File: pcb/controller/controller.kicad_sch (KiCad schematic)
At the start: 38 parts, among them J1 Barrel_Jack, J2 AVR-ISP-6, Q1 2N7002, U1 ATmega328P-A, Y1 Crystal_GND24

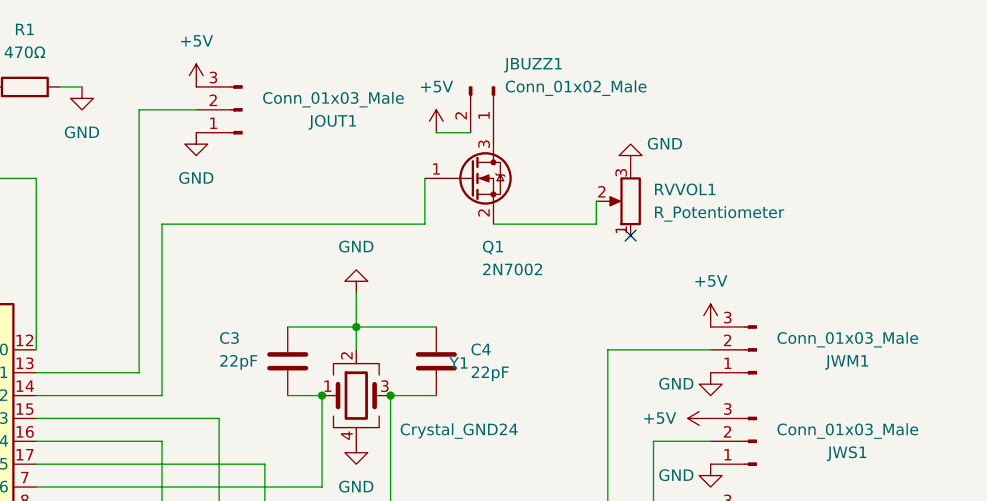
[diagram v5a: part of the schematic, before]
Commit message: PCB Touchup
Two changes in this commit.

1. I rewired the volume potentiometer so that the MOSFET is now the
closest thing to ground.  That way we'll always be sure to have
sufficient gate-source voltage to trigger it when the buzzer is turned
on.

2. I added v1/date indicators to the silk screen layers of all the
PCBs.
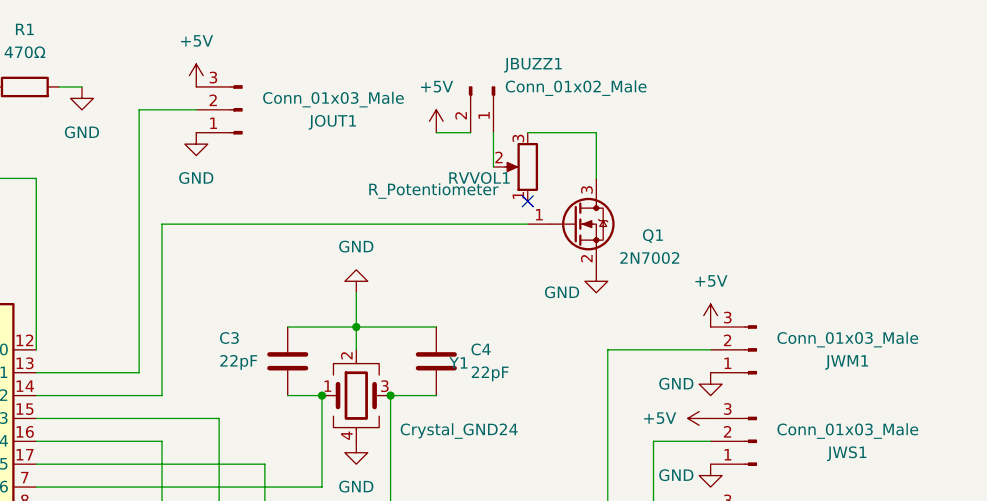
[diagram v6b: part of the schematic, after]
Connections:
- net GND: now also Q1.2 (S); no longer RVVOL1.3
- net at RVVOL1.2: now also JBUZZ1.1 (Pin_1); no longer Q1.2 (S)
- net at Q1.3 (D): now also RVVOL1.3; no longer JBUZZ1.1 (Pin_1)
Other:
- moved on the sheet: Q1, RVVOL1
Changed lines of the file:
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@@
   (junction (at 92.71 181.61) (diameter 0) (color 0 0 0 0)
   )
-  (no_connect (at 158.75 38.1))
+  (no_connect (at 147.32 34.29))
   (no_connect (at 25.4 50.8))
   (no_connect (at 62.23 58.42))
@@
     (stroke (width 0) (type default) (color 0 0 0 0))
   )
-  (wire (pts (xy 154.94 36.83) (xy 154.94 34.29))
-    (stroke (width 0) (type default) (color 0 0 0 0))
-  )
   (wire (pts (xy 124.46 128.27) (xy 121.92 128.27))
     (stroke (width 0) (type default) (color 0 0 0 0))
@@
     (stroke (width 0) (type default) (color 0 0 0 0))
   )
+  (wire (pts (xy 147.32 26.67) (xy 154.94 26.67))
+    (stroke (width 0) (type default) (color 0 0 0 0))
+  )
   (wire (pts (xy 106.68 156.21) (xy 106.68 162.56))
     (stroke (width 0) (type default) (color 0 0 0 0))
@@
     (stroke (width 0) (type default) (color 0 0 0 0))
   )
-  (wire (pts (xy 143.51 36.83) (xy 154.94 36.83))
-    (stroke (width 0) (type default) (color 0 0 0 0))
-  )
   (wire (pts (xy 132.08 68.58) (xy 132.08 55.88))
     (stroke (width 0) (type default) (color 0 0 0 0))
@@
     (stroke (width 0) (type default) (color 0 0 0 0))
   )
-  (wire (pts (xy 135.89 36.83) (xy 135.89 31.75))
+  (wire (pts (xy 143.51 26.67) (xy 143.51 30.48))
     (stroke (width 0) (type default) (color 0 0 0 0))
   )
@@
     (stroke (width 0) (type default) (color 0 0 0 0))
   )
+  (wire (pts (xy 154.94 26.67) (xy 154.94 31.75))
+    (stroke (width 0) (type default) (color 0 0 0 0))
+  )
   (wire (pts (xy 114.3 147.32) (xy 110.49 147.32))
     (stroke (width 0) (type default) (color 0 0 0 0))
@@
     (stroke (width 0) (type default) (color 0 0 0 0))
   )
-  (wire (pts (xy 106.68 36.83) (xy 135.89 36.83))
+  (wire (pts (xy 106.68 36.83) (xy 147.32 36.83))
     (stroke (width 0) (type default) (color 0 0 0 0))
   )
@@
     (pin "2")
   )
-  (symbol (lib_id "Device:R_Potentiometer") (at 158.75 34.29 180) (unit 1)
-    (in_bom yes) (on_board yes)
-    (property "Reference" "RVVOL1" (id 0) (at 161.29 33.0199 0)
+  (symbol (lib_id "Device:R_Potentiometer") (at 147.32 30.48 180) (unit 1)
+    (in_bom yes) (on_board yes)
+    (property "Reference" "RVVOL1" (id 0) (at 138.43 31.75 0)
       (effects (font (size 1.27 1.27)) (justify right))
     )
-    (property "Value" "R_Potentiometer" (id 1) (at 161.29 35.5599 0)
+    (property "Value" "R_Potentiometer" (id 1) (at 129.54 33.02 0)
       (effects (font (size 1.27 1.27)) (justify right))
     )
-    (property "Footprint" "Potentiometer_THT:Potentiometer_Bourns_3386P_Vertical" (id 2) (at 158.75 34.29 0)
-      (effects (font (size 1.27 1.27)) hide)
-    )
-    (property "Datasheet" "~" (id 3) (at 158.75 34.29 0)
+    (property "Footprint" "Potentiometer_THT:Potentiometer_Bourns_3386P_Vertical" (id 2) (at 147.32 30.48 0)
+      (effects (font (size 1.27 1.27)) hide)
+    )
+    (property "Datasheet" "~" (id 3) (at 147.32 30.48 0)
       (effects (font (size 1.27 1.27)) hide)
     )
@@
     (pin "1")
   )
-  (symbol (lib_id "Transistor_FET:2N7002") (at 140.97 31.75 0) (unit 1)
-    (in_bom yes) (on_board yes)
-    (property "Reference" "Q1" (id 0) (at 142.24 39.37 0)
-      (effects (font (size 1.27 1.27)) (justify left))
-    )
-    (property "Value" "2N7002" (id 1) (at 142.24 41.91 0)
-      (effects (font (size 1.27 1.27)) (justify left))
-    )
-    (property "Footprint" "Package_TO_SOT_SMD:SOT-23" (id 2) (at 146.05 33.655 0)
+  (symbol (lib_id "Transistor_FET:2N7002") (at 152.4 36.83 0) (unit 1)
+    (in_bom yes) (on_board yes)
+    (property "Reference" "Q1" (id 0) (at 160.02 38.1 0)
+      (effects (font (size 1.27 1.27)) (justify left))
+    )
+    (property "Value" "2N7002" (id 1) (at 157.48 40.64 0)
+      (effects (font (size 1.27 1.27)) (justify left))
+    )
+    (property "Footprint" "Package_TO_SOT_SMD:SOT-23" (id 2) (at 157.48 38.735 0)
       (effects (font (size 1.27 1.27) italic) (justify left) hide)
     )
-    (property "Datasheet" "https://www.onsemi.com/pub/Collateral/NDS7002A-D.PDF" (id 3) (at 140.97 31.75 0)
+    (property "Datasheet" "https://www.onsemi.com/pub/Collateral/NDS7002A-D.PDF" (id 3) (at 152.4 36.83 0)
       (effects (font (size 1.27 1.27)) (justify left) hide)
     )
-    (property "LCSC" "C8545" (id 4) (at 140.97 31.75 0)
+    (property "LCSC" "C8545" (id 4) (at 152.4 36.83 0)
       (effects (font (size 1.27 1.27)) hide)
     )
@@
     (pin "1")
   )
-  (symbol (lib_id "power:GND") (at 158.75 30.48 180) (unit 1)
-    (in_bom yes) (on_board yes)
-    (property "Reference" "#PWR0140" (id 0) (at 158.75 24.13 0)
-      (effects (font (size 1.27 1.27)) hide)
-    )
-    (property "Value" "GND" (id 1) (at 162.56 27.94 0))
-    (property "Footprint" "" (id 2) (at 158.75 30.48 0)
-      (effects (font (size 1.27 1.27)) hide)
-    )
-    (property "Datasheet" "" (id 3) (at 158.75 30.48 0)
-      (effects (font (size 1.27 1.27)) hide)
-    )
+  (symbol (lib_id "power:GND") (at 154.94 41.91 0) (unit 1)
+    (in_bom yes) (on_board yes)
+    (property "Reference" "#PWR0140" (id 0) (at 154.94 48.26 0)
+      (effects (font (size 1.27 1.27)) hide)
+    )
+    (property "Value" "GND" (id 1) (at 151.13 44.45 0))
+    (property "Footprint" "" (id 2) (at 154.94 41.91 0)
+      (effects (font (size 1.27 1.27)) hide)
+    )
+    (property "Datasheet" "" (id 3) (at 154.94 41.91 0)
+      (effects (font (size 1.27 1.27)) hide)
+    )

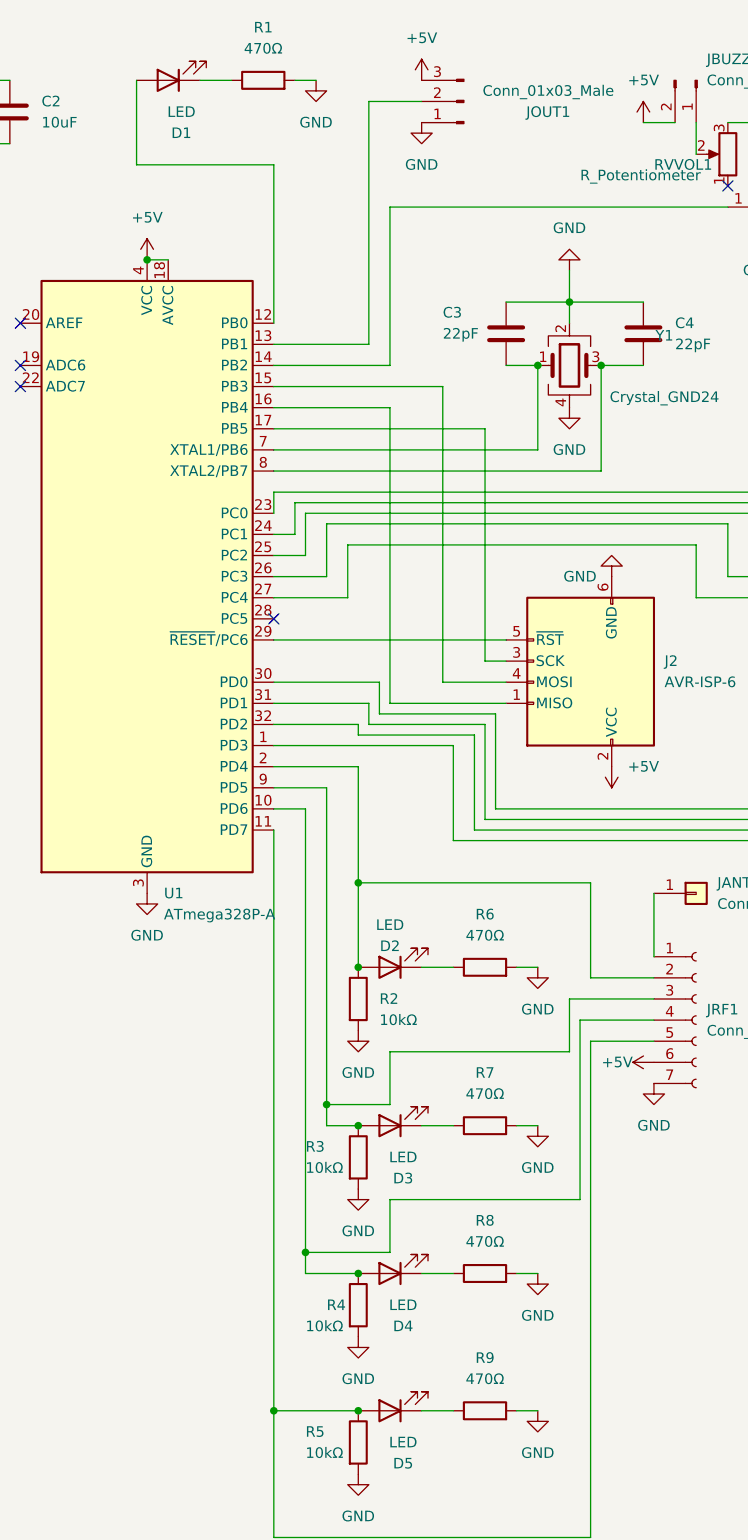
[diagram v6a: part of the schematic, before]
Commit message: Bump Up LED Resistors
The LEDs on the controller board are very bright in the first batch of
boards, so this replaces the 470ohm resistors with 1k resistors to dim
them a little.
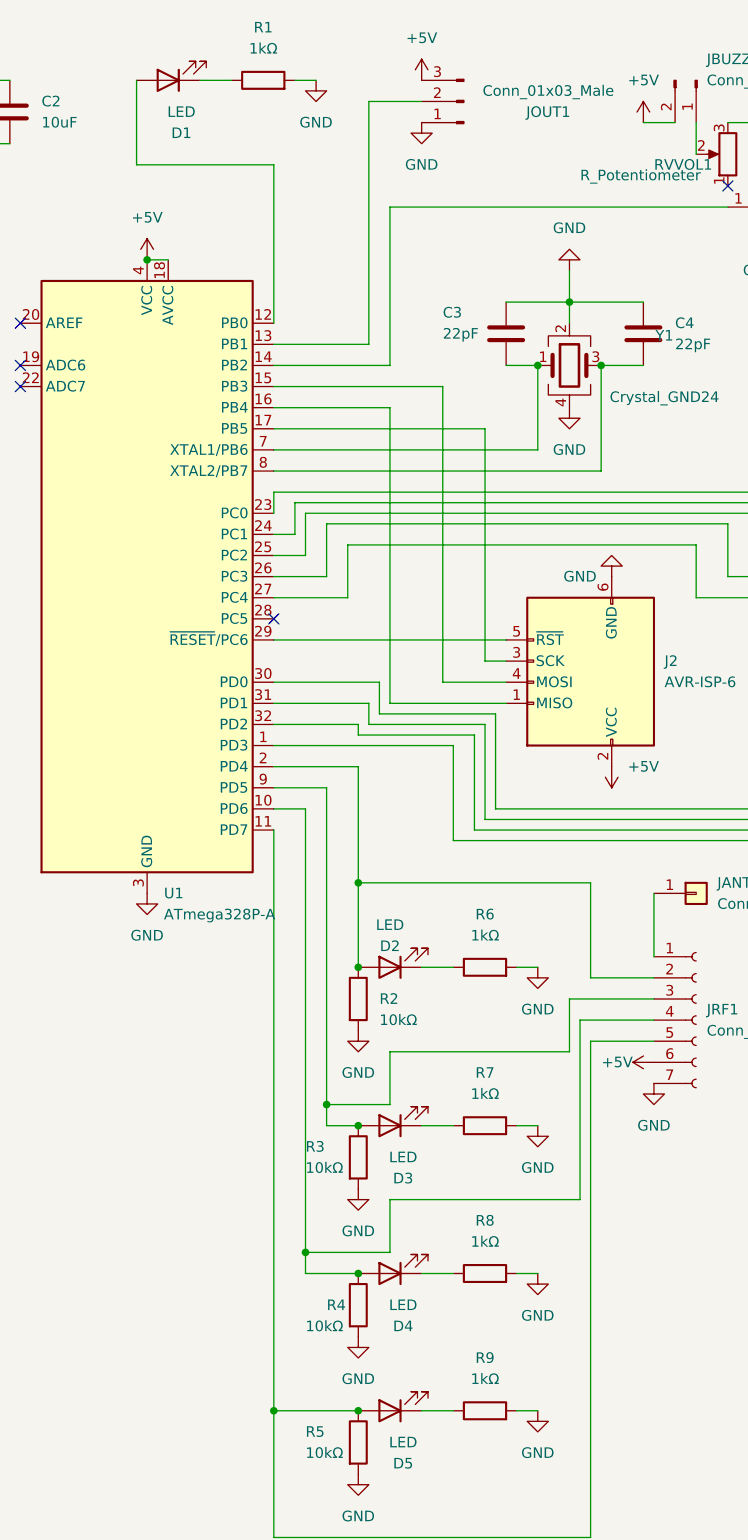
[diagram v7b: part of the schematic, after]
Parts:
- R1, R6, R7, R8, R9: value 470Ω -> 1kΩ; footprint Resistor_SMD:R_0805_2012Metric -> Resistor_SMD:R_0603_1608Metric; LCSC C17710 -> C21190
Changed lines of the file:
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@@
     (pin "3")
+  )
+  (symbol (lib_id "Device:R") (at 118.11 128.27 90) (unit 1)
+    (in_bom yes) (on_board yes) (fields_autoplaced)
+    (property "Reference" "R6" (id 0) (at 118.11 121.92 90))
+    (property "Value" "1kΩ" (id 1) (at 118.11 124.46 90))
+    (property "Footprint" "Resistor_SMD:R_0603_1608Metric" (id 2) (at 118.11 130.048 90)
+      (effects (font (size 1.27 1.27)) hide)
+    )
+    (property "Datasheet" "~" (id 3) (at 118.11 128.27 0)
+      (effects (font (size 1.27 1.27)) hide)
+    )
+    (property "LCSC" "C21190" (id 4) (at 118.11 128.27 90)
+      (effects (font (size 1.27 1.27)) hide)
+    )
+    (pin "1")
+    (pin "2")
   )
   (symbol (lib_id "power:+5V") (at 77.47 43.18 0) (unit 1)
@@
     (pin "3")
   )
-  (symbol (lib_id "Device:R") (at 118.11 165.1 90) (unit 1)
-    (in_bom yes) (on_board yes) (fields_autoplaced)
-    (property "Reference" "R8" (id 0) (at 118.11 158.75 90))
-    (property "Value" "470Ω" (id 1) (at 118.11 161.29 90))
-    (property "Footprint" "Resistor_SMD:R_0805_2012Metric" (id 2) (at 118.11 166.878 90)
-      (effects (font (size 1.27 1.27)) hide)
-    )
-    (property "Datasheet" "~" (id 3) (at 118.11 165.1 0)
-      (effects (font (size 1.27 1.27)) hide)
-    )
-    (property "LCSC" "C17710" (id 4) (at 118.11 165.1 90)
-      (effects (font (size 1.27 1.27)) hide)
-    )
-    (pin "1")
-    (pin "2")
-  )
   (symbol (lib_id "power:GND") (at 138.43 142.24 0) (unit 1)
     (in_bom yes) (on_board yes) (fields_autoplaced)
@@
     )
     (pin "1")
-  )
-  (symbol (lib_id "Device:R") (at 118.11 147.32 90) (unit 1)
-    (in_bom yes) (on_board yes) (fields_autoplaced)
-    (property "Reference" "R7" (id 0) (at 118.11 140.97 90))
-    (property "Value" "470Ω" (id 1) (at 118.11 143.51 90))
-    (property "Footprint" "Resistor_SMD:R_0805_2012Metric" (id 2) (at 118.11 149.098 90)
-      (effects (font (size 1.27 1.27)) hide)
-    )
-    (property "Datasheet" "~" (id 3) (at 118.11 147.32 0)
-      (effects (font (size 1.27 1.27)) hide)
-    )
-    (property "LCSC" "C17710" (id 4) (at 118.11 147.32 90)
-      (effects (font (size 1.27 1.27)) hide)
-    )
-    (pin "1")
-    (pin "2")
   )
   (symbol (lib_id "power:GND") (at 167.64 73.66 0) (unit 1)
@@
     (pin "1")
   )
-  (symbol (lib_id "Device:R") (at 118.11 181.61 90) (unit 1)
-    (in_bom yes) (on_board yes) (fields_autoplaced)
-    (property "Reference" "R9" (id 0) (at 118.11 175.26 90))
-    (property "Value" "470Ω" (id 1) (at 118.11 177.8 90))
-    (property "Footprint" "Resistor_SMD:R_0805_2012Metric" (id 2) (at 118.11 183.388 90)
-      (effects (font (size 1.27 1.27)) hide)
-    )
-    (property "Datasheet" "~" (id 3) (at 118.11 181.61 0)
-      (effects (font (size 1.27 1.27)) hide)
-    )
-    (property "LCSC" "C17710" (id 4) (at 118.11 181.61 90)
-      (effects (font (size 1.27 1.27)) hide)
-    )
-    (pin "1")
-    (pin "2")
-  )
   (symbol (lib_id "Device:R_Potentiometer") (at 147.32 30.48 180) (unit 1)
     (in_bom yes) (on_board yes)
@@
     (in_bom yes) (on_board yes) (fields_autoplaced)
     (property "Reference" "R1" (id 0) (at 91.44 15.24 90))
-    (property "Value" "470Ω" (id 1) (at 91.44 17.78 90))
-    (property "Footprint" "Resistor_SMD:R_0805_2012Metric" (id 2) (at 91.44 23.368 90)
+    (property "Value" "1kΩ" (id 1) (at 91.44 17.78 90))
+    (property "Footprint" "Resistor_SMD:R_0603_1608Metric" (id 2) (at 91.44 23.368 90)
       (effects (font (size 1.27 1.27)) hide)
     )
@@
       (effects (font (size 1.27 1.27)) hide)
     )
-    (property "LCSC" "C17710" (id 4) (at 91.44 21.59 90)
+    (property "LCSC" "C21190" (id 4) (at 91.44 21.59 90)
       (effects (font (size 1.27 1.27)) hide)
     )
@@
     )
     (property "Datasheet" "~" (id 3) (at 143.51 21.59 0)
+      (effects (font (size 1.27 1.27)) hide)
+    )
+    (pin "1")
+    (pin "2")
+  )
+  (symbol (lib_id "Device:R") (at 118.11 165.1 90) (unit 1)
+    (in_bom yes) (on_board yes) (fields_autoplaced)
+    (property "Reference" "R8" (id 0) (at 118.11 158.75 90))
+    (property "Value" "1kΩ" (id 1) (at 118.11 161.29 90))
+    (property "Footprint" "Resistor_SMD:R_0603_1608Metric" (id 2) (at 118.11 166.878 90)
+      (effects (font (size 1.27 1.27)) hide)
+    )
+    (property "Datasheet" "~" (id 3) (at 118.11 165.1 0)
+      (effects (font (size 1.27 1.27)) hide)
+    )
+    (property "LCSC" "C21190" (id 4) (at 118.11 165.1 90)
       (effects (font (size 1.27 1.27)) hide)
     )
@@
     (pin "1")
   )
-  (symbol (lib_id "Device:R") (at 118.11 128.27 90) (unit 1)
-    (in_bom yes) (on_board yes) (fields_autoplaced)
-    (property "Reference" "R6" (id 0) (at 118.11 121.92 90))
-    (property "Value" "470Ω" (id 1) (at 118.11 124.46 90))
-    (property "Footprint" "Resistor_SMD:R_0805_2012Metric" (id 2) (at 118.11 130.048 90)
-      (effects (font (size 1.27 1.27)) hide)
-    )
-    (property "Datasheet" "~" (id 3) (at 118.11 128.27 0)
-      (effects (font (size 1.27 1.27)) hide)
-    )
-    (property "LCSC" "C17710" (id 4) (at 118.11 128.27 90)
-      (effects (font (size 1.27 1.27)) hide)
-    )
-    (pin "1")
-    (pin "2")
-  )
   (symbol (lib_id "power:+5V") (at 137.16 26.67 0) (unit 1)
     (in_bom yes) (on_board yes) (fields_autoplaced)
@@
     (pin "3")
   )
+  (symbol (lib_id "Device:R") (at 118.11 147.32 90) (unit 1)
+    (in_bom yes) (on_board yes) (fields_autoplaced)
+    (property "Reference" "R7" (id 0) (at 118.11 140.97 90))
+    (property "Value" "1kΩ" (id 1) (at 118.11 143.51 90))
+    (property "Footprint" "Resistor_SMD:R_0603_1608Metric" (id 2) (at 118.11 149.098 90)
+      (effects (font (size 1.27 1.27)) hide)
+    )
+    (property "Datasheet" "~" (id 3) (at 118.11 147.32 0)
+      (effects (font (size 1.27 1.27)) hide)
+    )
+    (property "LCSC" "C21190" (id 4) (at 118.11 147.32 90)
+      (effects (font (size 1.27 1.27)) hide)
+    )
+    (pin "1")
+    (pin "2")
+  )
   (symbol (lib_id "Device:R") (at 102.87 151.13 0) (unit 1)
     (in_bom yes) (on_board yes)
@@
     )
     (property "Datasheet" "~" (id 3) (at 29.21 26.416 0)
+      (effects (font (size 1.27 1.27)) hide)
+    )
+    (pin "1")
+    (pin "2")
+  )
+  (symbol (lib_id "Device:R") (at 118.11 181.61 90) (unit 1)
+    (in_bom yes) (on_board yes) (fields_autoplaced)
+    (property "Reference" "R9" (id 0) (at 118.11 175.26 90))
+    (property "Value" "1kΩ" (id 1) (at 118.11 177.8 90))
+    (property "Footprint" "Resistor_SMD:R_0603_1608Metric" (id 2) (at 118.11 183.388 90)
+      (effects (font (size 1.27 1.27)) hide)
+    )
+    (property "Datasheet" "~" (id 3) (at 118.11 181.61 0)
+      (effects (font (size 1.27 1.27)) hide)
+    )
+    (property "LCSC" "C21190" (id 4) (at 118.11 181.61 90)
       (effects (font (size 1.27 1.27)) hide)
     )
@@
     )
     (path "/50b4d9f0-1a5d-4592-8fa5-c4c991413255"
-      (reference "R1") (unit 1) (value "470Ω") (footprint "Resistor_SMD:R_0805_2012Metric")
+      (reference "R1") (unit 1) (value "1kΩ") (footprint "Resistor_SMD:R_0603_1608Metric")
     )
     (path "/d2d13151-4e30-4405-9d5f-9b9711d0687b"
@@
       (reference "R5") (unit 1) (value "10kΩ") (footprint "Resistor_SMD:R_0603_1608Metric")
     )
-    (path "/9adaeaa2-9a90-4c48-b554-075117905012"
-      (reference "R6") (unit 1) (value "470Ω") (footprint "Resistor_SMD:R_0805_2012Metric")
-    )
-    (path "/3352e9eb-5ba7-4ce1-a6e5-125a48c39e4b"
-      (reference "R7") (unit 1) (value "470Ω") (footprint "Resistor_SMD:R_0805_2012Metric")
-    )
-    (path "/2f812da1-e031-4173-9c00-91e33beee6ca"
-      (reference "R8") (unit 1) (value "470Ω") (footprint "Resistor_SMD:R_0805_2012Metric")
-    )
-    (path "/4c090123-115c-4d08-bf2b-5f241a519cbb"
-      (reference "R9") (unit 1) (value "470Ω") (footprint "Resistor_SMD:R_0805_2012Metric")
+    (path "/2515592d-6550-47b7-aa06-fd7fd0ec82ae"
+      (reference "R6") (unit 1) (value "1kΩ") (footprint "Resistor_SMD:R_0603_1608Metric")
+    )
+    (path "/b52f1af8-299f-4ede-92cb-8b540c7f07ef"
+      (reference "R7") (unit 1) (value "1kΩ") (footprint "Resistor_SMD:R_0603_1608Metric")
+    )
+    (path "/6769f420-db96-4663-83af-700fffd703ad"
+      (reference "R8") (unit 1) (value "1kΩ") (footprint "Resistor_SMD:R_0603_1608Metric")
+    )
+    (path "/cab90745-d567-4a37-b941-b5d1bb4dc2b9"
+      (reference "R9") (unit 1) (value "1kΩ") (footprint "Resistor_SMD:R_0603_1608Metric")
     )
     (path "/90473c38-5d7d-4dc8-a497-0758a521fafc"
